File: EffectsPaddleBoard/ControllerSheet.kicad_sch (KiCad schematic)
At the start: 1 part, among them U1 STM32F446RETx

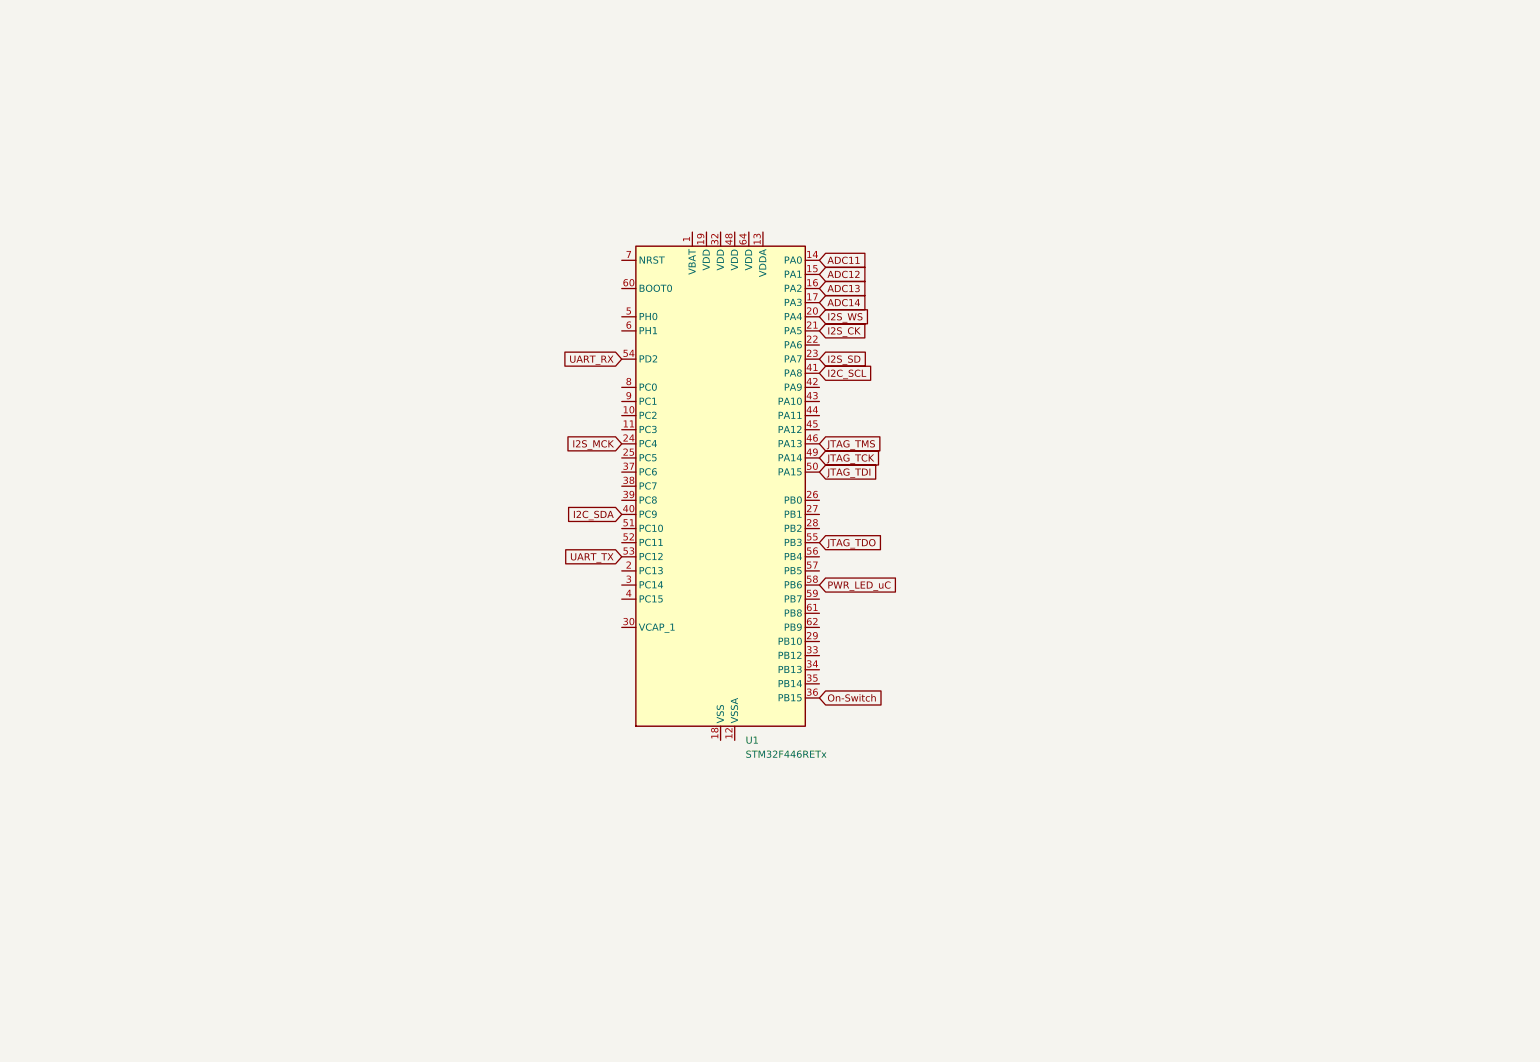
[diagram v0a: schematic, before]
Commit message: Added power to uC, but overall power not finished
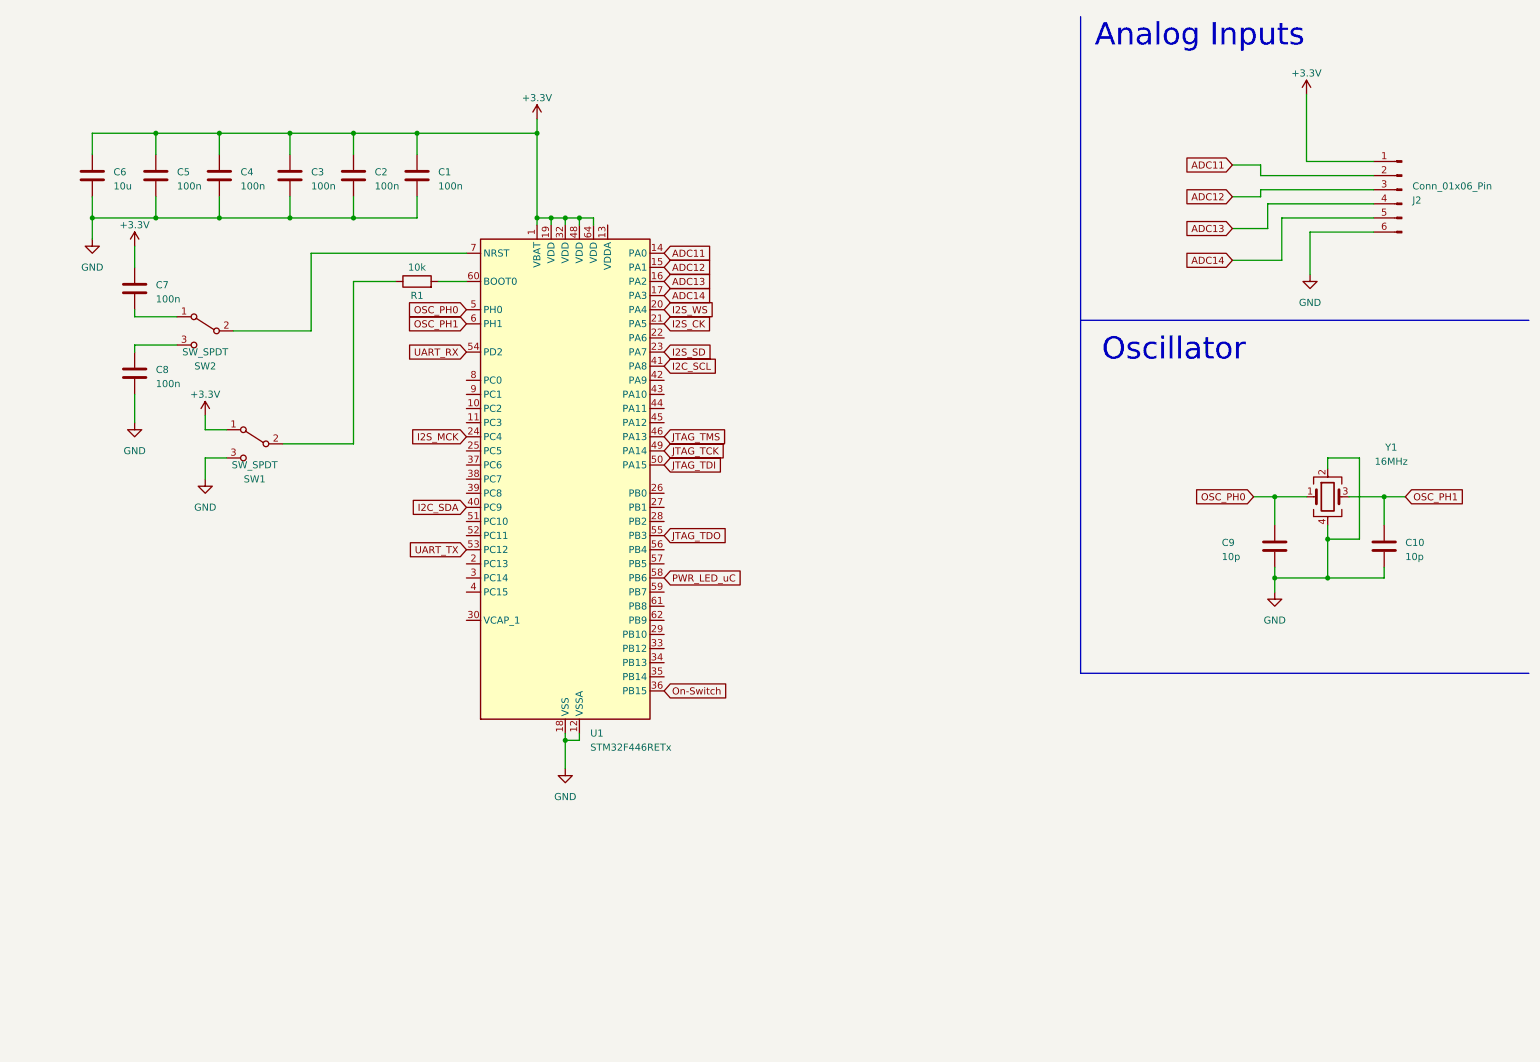
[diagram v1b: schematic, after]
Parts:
- added C1, C2, C3, C4, C5, C7, C8: 100n, symbol Device:C
- added C10, C9: 10p, symbol Device:C
- added C6: 10u, symbol Device:C
- added J2: Conn_01x06_Pin, symbol Connector:Conn_01x06_Pin
- added R1: 10k, symbol Device:R
- added SW1, SW2: SW_SPDT, symbol Switch:SW_SPDT
- added Y1: 16MHz, symbol Device:Crystal_GND24
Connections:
- net ADC11: now also J2.2 (Pin_2)
- net ADC12: now also J2.3 (Pin_3)
- net ADC13: now also J2.4 (Pin_4)
- net ADC14: now also J2.5 (Pin_5)
- net +3.3V: now reaches U1.1 (VBAT)
- net +3.3V: now also U1.19 (VDD), U1.32 (VDD), U1.48 (VDD), U1.64 (VDD), C1.1, C2.1, C3.1, C4.1, C5.1, C6.1, C7.1, J2.1 (Pin_1), SW1.1 (A)
- net GND: now reaches U1.12 (VSSA)
- net GND: now also U1.18 (VSS), U1.31 (VSS), U1.47 (VSS), U1.63 (VSS), C1.2, C10.2, C2.2, C3.2, C4.2, C5.2, C6.2, C8.2, C9.2, J2.6 (Pin_6), SW1.3 (C), Y1.2, Y1.4
- net OSC_PH0: now reaches U1.5 (PH0)
- net OSC_PH0: now also C9.1, Y1.1
- net OSC_PH1: now reaches U1.6 (PH1)
- net OSC_PH1: now also C10.1, Y1.3
- net at U1.60 (BOOT0): now also R1.2
- net at U1.7 (NRST): now also SW2.2 (B)
- new net: C8.1, SW2.3 (C)
- new net: R1.1, SW1.2 (B)
- new net: C7.2, SW2.1 (A)
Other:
- note added: "Analog Inputs"
- note added: "Oscillator"
- company: (none) -> Selbstständig
- title: (none) -> Effects Paddle
- moved on the sheet: U1

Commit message: While wiring the codec, I found that I used the wrong controller and so I2S communication is unidirectional only: TODO: fix that
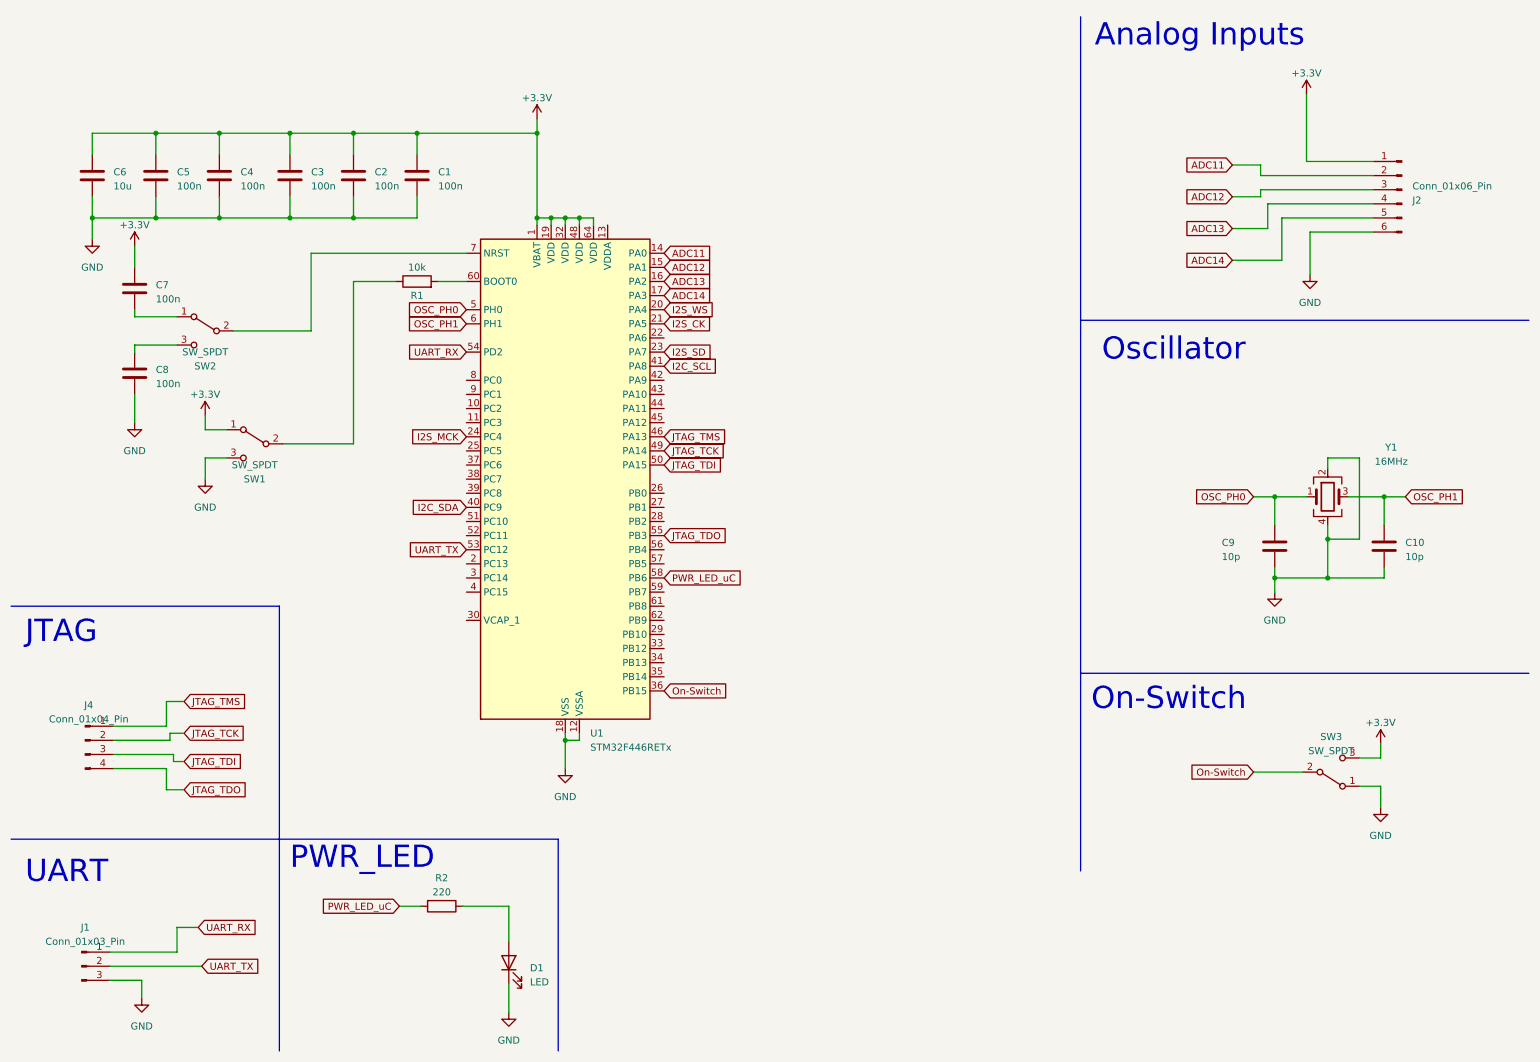
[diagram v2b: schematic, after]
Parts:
- added D1: LED, symbol Device:LED
- added J1: Conn_01x03_Pin, symbol Connector:Conn_01x03_Pin
- added J4: Conn_01x04_Pin, symbol Connector:Conn_01x04_Pin
- added R2: 220, symbol Device:R
- added SW3: SW_SPDT, symbol Switch:SW_SPDT
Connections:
- net +3.3V: now also SW3.3 (C)
- net GND: now also D1.1 (K), J1.3 (Pin_3), SW3.1 (A)
- net JTAG_TCK: now also J4.2 (Pin_2)
- net JTAG_TDI: now also J4.3 (Pin_3)
- net JTAG_TDO: now also J4.4 (Pin_4)
- net JTAG_TMS: now also J4.1 (Pin_1)
- net On-Switch: now also SW3.2 (B)
- net PWR_LED_uC: now also R2.2
- net UART_RX: now also J1.1 (Pin_1)
- net UART_TX: now also J1.2 (Pin_2)
- new net: D1.2 (A), R2.1
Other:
- note added: "JTAG"
- note added: "On-Switch"
- note added: "PWR_LED"
- note added: "UART"

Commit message: Added power supply
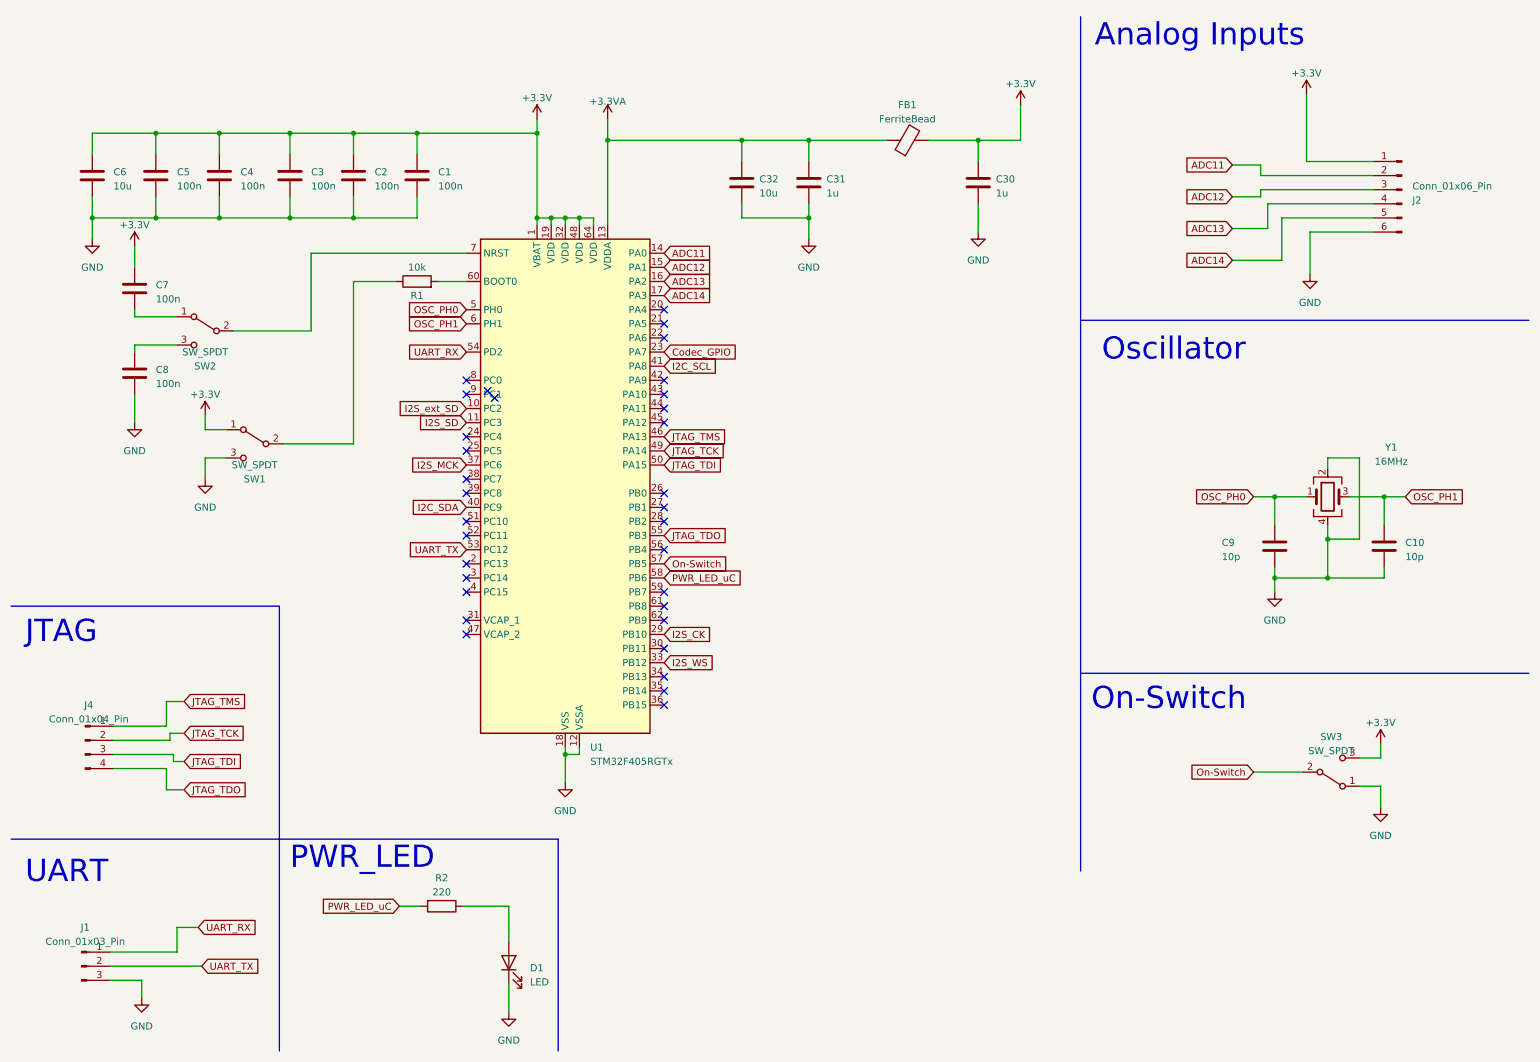
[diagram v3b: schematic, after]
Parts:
- removed U1: STM32F446RETx, Package_QFP:LQFP-64_10x10mm_P0.5mm, symbol MCU_ST_STM32F4:STM32F446RETx
- added C30, C31: 1u, symbol Device:C
- added C32: 10u, symbol Device:C
- added FB1: FerriteBead, symbol Device:FerriteBead
- added U1: STM32F405RGTx, Package_QFP:LQFP-64_10x10mm_P0.5mm, symbol MCU_ST_STM32F4:STM32F405RGTx
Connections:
- net +3.3V: now also C30.1, FB1.2, U1.1 (VBAT), U1.19 (VDD), U1.32 (VDD), U1.48 (VDD), U1.64 (VDD)
- net ADC11: now also U1.14 (PA0)
- net ADC12: now also U1.15 (PA1)
- net ADC13: now also U1.16 (PA2)
- net ADC14: now also U1.17 (PA3)
- net GND: now also C30.2, C31.2, C32.2, U1.12 (VSSA), U1.18 (VSS), U1.63 (VSS)
- net I2C_SCL: now also U1.41 (PA8)
- net I2C_SDA: now also U1.40 (PC9)
- net I2S_CK: now also U1.29 (PB10)
- net I2S_MCK: now also U1.37 (PC6)
- net I2S_SD: now also U1.11 (PC3)
- net I2S_WS: now also U1.33 (PB12)
- net JTAG_TCK: now also U1.49 (PA14)
- net JTAG_TDI: now also U1.50 (PA15)
- net JTAG_TDO: now also U1.55 (PB3)
- net JTAG_TMS: now also U1.46 (PA13)
- net OSC_PH0: now also U1.5 (PH0)
- net OSC_PH1: now also U1.6 (PH1)
- net On-Switch: now also U1.57 (PB5)
- net PWR_LED_uC: now also U1.58 (PB6)
- net UART_RX: now also U1.54 (PD2)
- net UART_TX: now also U1.53 (PC12)
- net at R1.2: now also U1.60 (BOOT0)
- net at SW2.2 (B): now also U1.7 (NRST)
- new net +3.3VA: C31.1, C32.1, FB1.1, U1.13 (VDDA)
- new net Codec_GPIO: U1.23 (PA7)
- new net I2S_ext_SD: U1.10 (PC2)
- no-connect marks 0 -> 33

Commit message: Finished schematic
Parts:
- removed C30, C31: 1u, symbol Device:C
- removed C32: 10u, symbol Device:C
- removed FB1: FerriteBead, symbol Device:FerriteBead
